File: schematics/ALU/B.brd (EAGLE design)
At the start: 28.1 x 43 mm, 8 parts

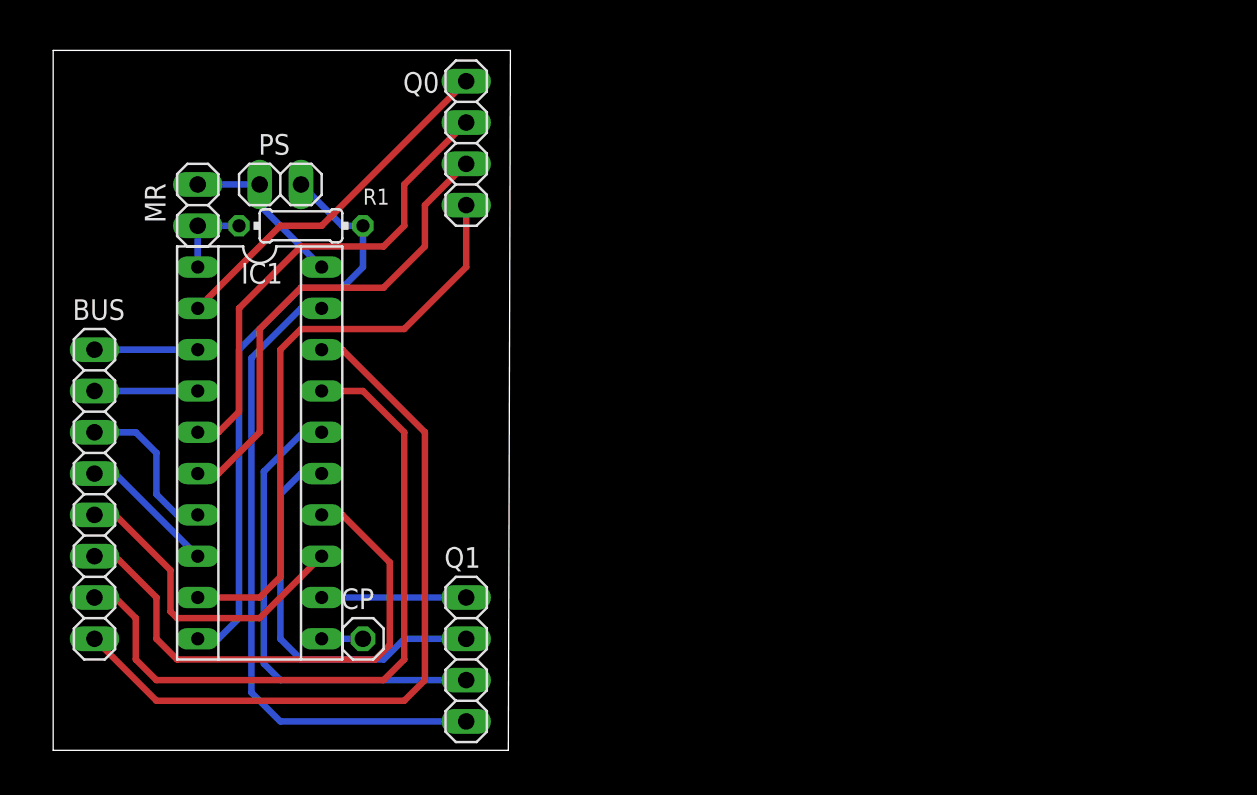
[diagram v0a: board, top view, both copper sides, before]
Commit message: Added sch and brd for ALU-B, sch, brd and gerber for pc register.
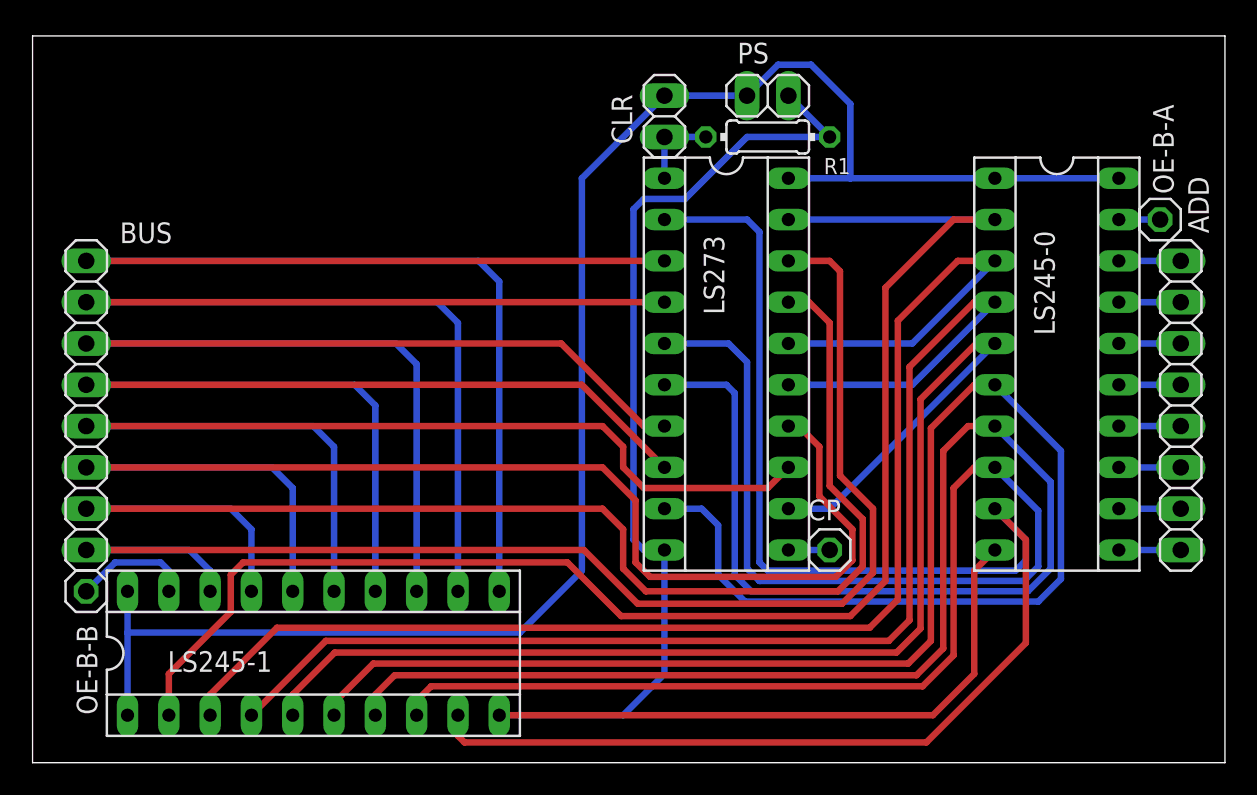
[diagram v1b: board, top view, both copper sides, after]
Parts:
- removed IC1: (no value), ic-package:SOCKET-20
- removed MR: (no value), pinhead:1X02
- removed Q0, Q1: (no value), pinhead:1X04
- added ADD: (no value), pinhead:1X08
- added CLR: (no value), pinhead:1X02
- added LS245-0, LS245-1, LS273: (no value), ic-package:SOCKET-20
- added OE-B-A, OE-B-B: (no value), pinhead:1X01
- moved PS 30.5 mm to (45.2, 41.0)
- moved R1 29.2 mm to (45.2, 38.5), turned to 180 degrees
- moved CP 29.2 mm to (49.0, 13.1)
- moved BUS 5.48 mm to (3.30, 22.0)
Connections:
- removed net D0: BUS.8, IC1.3
- removed net D1: BUS.7, IC1.4
- removed net D2: BUS.6, IC1.7
- removed net D3: BUS.5, IC1.8
- removed net D4: BUS.4, IC1.13
- removed net D5: BUS.3, IC1.14
- removed net D6: BUS.2, IC1.17
- removed net D7: BUS.1, IC1.18
- new net A0: ADD.1, LS245-0.18
- new net A1: ADD.2, LS245-0.17
- new net A2: ADD.3, LS245-0.16
- new net A3: ADD.4, LS245-0.15
- new net A4: ADD.5, LS245-0.14
- new net A5: ADD.6, LS245-0.13
- new net A6: ADD.7, LS245-0.12
- new net A7: ADD.8, LS245-0.11
- new net B-A: LS245-0.19, OE-B-A.1
- new net B-B: LS245-1.19, OE-B-B.1
- new net B0: BUS.8, LS245-1.11, LS273.3
- new net B1: BUS.7, LS245-1.12, LS273.4
- new net B2: BUS.6, LS245-1.13, LS273.7
- new net B3: BUS.5, LS245-1.14, LS273.8
- new net B4: BUS.4, LS245-1.15, LS273.13
- new net B5: BUS.3, LS245-1.16, LS273.14
- new net B6: BUS.2, LS245-1.17, LS273.17
- new net B7: BUS.1, LS245-1.18, LS273.18
- net CLR: now also CLR.2, LS273.1, R1.2; no longer IC1.1, MR.2, R1.1
- net CP: now also LS273.11; no longer IC1.11
- net GND: now also LS245-0.10, LS245-1.10, LS273.10, R1.1; no longer IC1.10, R1.2
- net Q0: now also LS245-0.9, LS245-1.9, LS273.2; no longer IC1.2, Q0.1
- net Q1: now also LS245-0.8, LS245-1.8, LS273.5; no longer IC1.5, Q0.2
- net Q2: now also LS245-0.7, LS245-1.7, LS273.6; no longer IC1.6, Q0.3
- net Q3: now also LS245-0.6, LS245-1.6, LS273.9; no longer IC1.9, Q0.4
- net Q4: now also LS245-0.5, LS245-1.5, LS273.12; no longer IC1.12, Q1.1
- net Q5: now also LS245-0.4, LS245-1.4, LS273.15; no longer IC1.15, Q1.2
- net Q6: now also LS245-0.3, LS245-1.3, LS273.16; no longer IC1.16, Q1.3
- net Q7: now also LS245-0.2, LS245-1.2, LS273.19; no longer IC1.19, Q1.4
- net VCC: now also CLR.1, LS245-0.1, LS245-0.20, LS245-1.1, LS245-1.20, LS273.20; no longer IC1.20, MR.1
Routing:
- net VCC: track 10.5 -> 106.6 mm
- net B6: track 0.00 -> 85.3 mm
- net B7: track 0.00 -> 82.8 mm
- net B5: track 0.00 -> 82.4 mm
- net B0: track 0.00 -> 80.5 mm
- net B1: track 0.00 -> 75.5 mm
- net Q0: track 22.3 -> 95.2 mm
- net B2: track 0.00 -> 72.5 mm
- net B4: track 0.00 -> 70.7 mm
- net Q2: track 29.6 -> 99.6 mm
- net Q4: track 8.89 -> 78.6 mm
- net B3: track 0.00 -> 67.4 mm
- net Q3: track 36.9 -> 99.9 mm
- net Q1: track 29.6 -> 92.5 mm
- net GND: track 36.7 -> 97.2 mm
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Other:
- board size 28.1 x 43 mm -> 73.3 x 44.7 mm
